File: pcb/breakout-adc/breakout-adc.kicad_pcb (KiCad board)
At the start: 4 copper layers, 100 x 62 mm, 107 parts, among them J1 Screw_Terminal_01x04, J10 Black, J11 Conn_02x06_Pin, J12 Conn_02x06_Pin, J13 Red, J14 Black, J15 FX18-120P-0.8SV20, J16 Black, J17 Black, J18 Black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

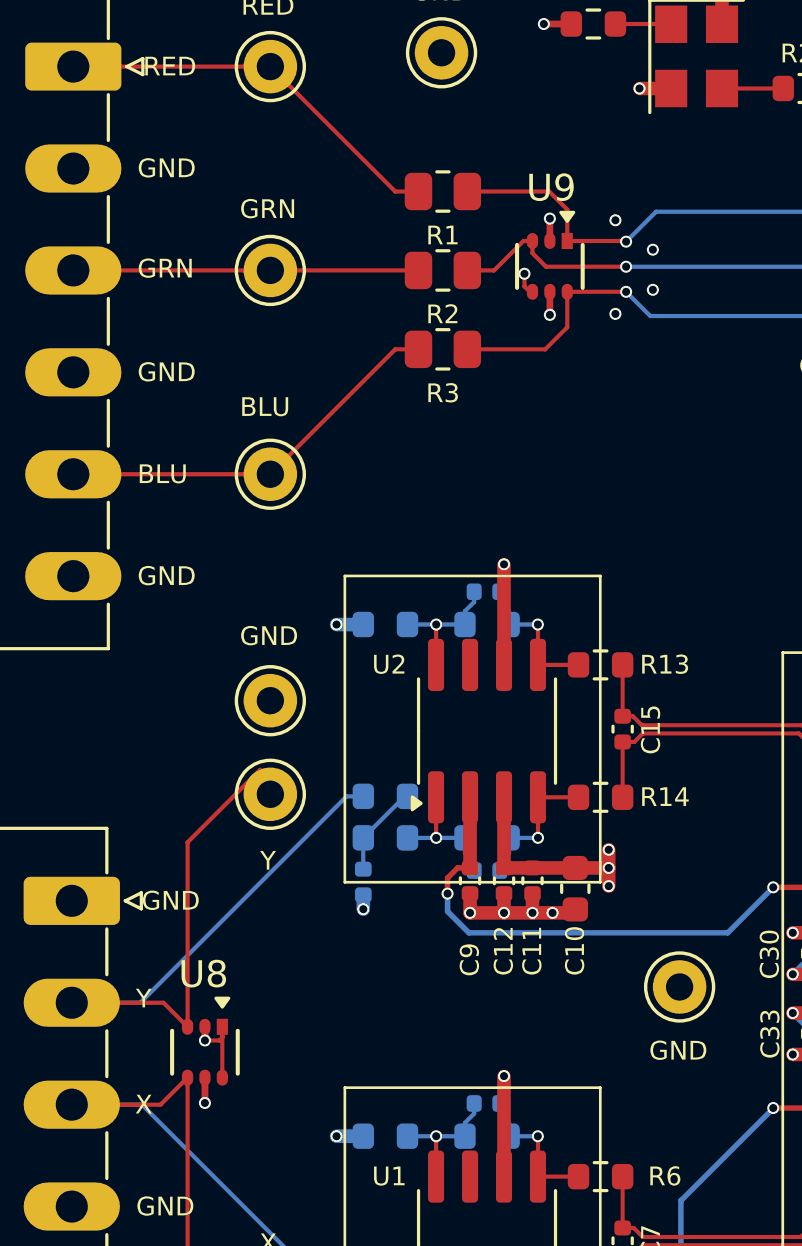
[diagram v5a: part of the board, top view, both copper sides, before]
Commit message: [adc][pcb] add esd datasheet
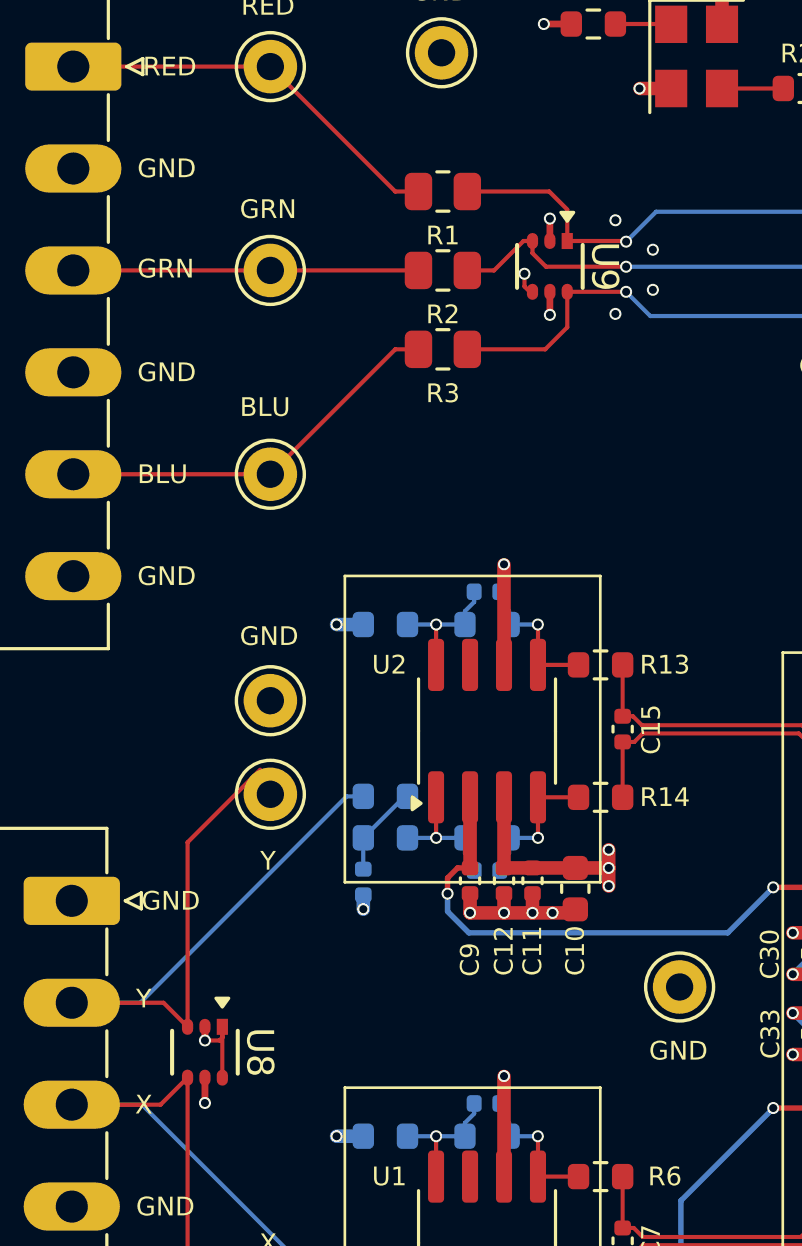
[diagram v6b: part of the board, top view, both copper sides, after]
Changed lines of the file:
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@@
 		(tags "D1213A-04S-7 ")
 		(property "Reference" "U8"
-			(at -2.903026 0.054509 0)
+			(at 0 -2.05 -90)
 			(unlocked yes)
 			(layer "F.SilkS")
@@
 			)
 		)
-		(property "Footprint" "D1213A:SOT-363_DIO"
-			(at 0 0 90)
+		(property "Footprint" "SOT-363_DIO"
+			(at 0 0 -90)
 			(layer "F.Fab")
 			(hide yes)
@@
 			)
 		)
-		(property "Datasheet" "D1213A-04S-7"
-			(at 0 0 90)
+		(property "Datasheet" "https://www.diodes.com/assets/Datasheets/D1213A-04S.pdf"
+			(at 0 0 -90)
 			(layer "F.Fab")
 			(hide yes)
@@
 		)
 		(property "Description" ""
-			(at 0 0 90)
+			(at 0 0 -90)
 			(layer "F.Fab")
 			(hide yes)
@@
 		(tags "D1213A-04S-7 ")
 		(property "Reference" "U9"
-			(at -2.925 -0.049999 0)
+			(at 0 -2.05 -90)
 			(unlocked yes)
 			(layer "F.SilkS")
@@
 			)
 		)
-		(property "Footprint" "D1213A:SOT-363_DIO"
-			(at 0 0 90)
+		(property "Footprint" "SOT-363_DIO"
+			(at 0 0 -90)
 			(layer "F.Fab")
 			(hide yes)
@@
 			)
 		)
-		(property "Datasheet" "D1213A-04S-7"
-			(at 0 0 90)
+		(property "Datasheet" "https://www.diodes.com/assets/Datasheets/D1213A-04S.pdf"
+			(at 0 0 -90)
 			(layer "F.Fab")
 			(hide yes)
@@
 		)
 		(property "Description" ""
-			(at 0 0 90)
+			(at 0 0 -90)
 			(layer "F.Fab")
 			(hide yes)
